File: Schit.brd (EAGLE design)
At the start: 58.1 x 47 mm, 15 parts, among them IC2 MEGA16-A, Q1 12M

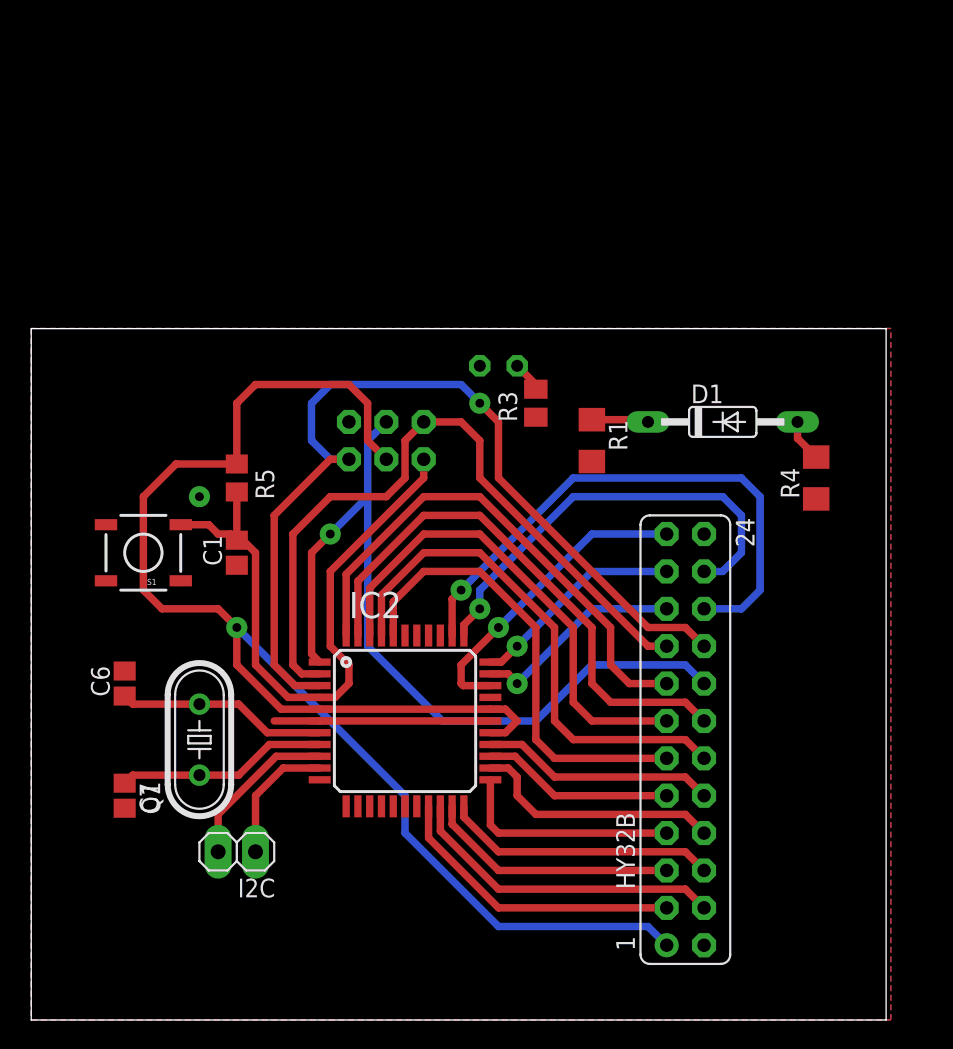
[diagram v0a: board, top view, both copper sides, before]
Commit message: change mc to ATMega64A
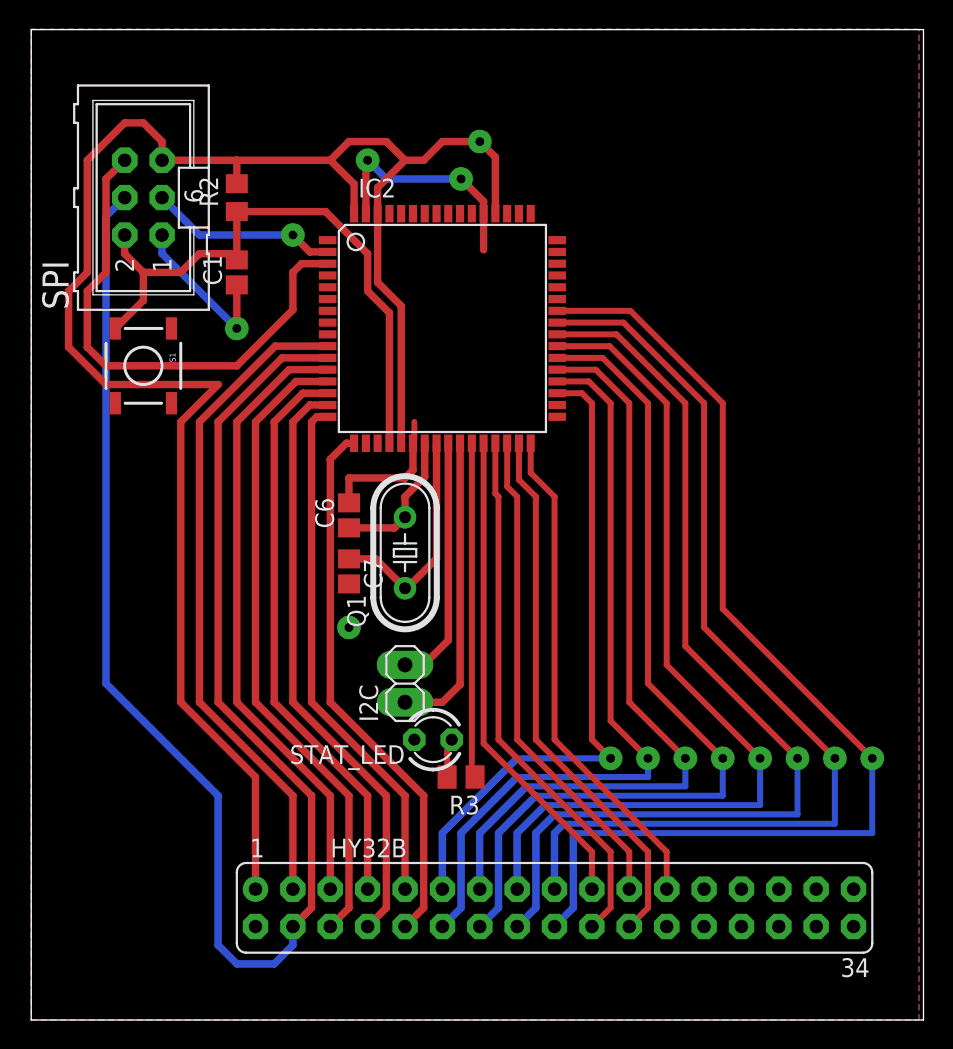
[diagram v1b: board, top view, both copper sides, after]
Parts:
- removed D1: 1N4446, diode:DO35-10
- removed R1: 220, resistor:R1206
- removed R4: 20, resistor:R1206
- removed R5: 10k, rcl:R0805
- added R2: 10k, rcl:R0805
- HY32B: device con-lsta:FE12-2 -> con-lsta:FE17-2
- IC2: value MEGA16-A -> MEGA64-A; device atmel:TQFP44 -> atmel:TQFP64
- moved IC2 26.8 mm to (27.9, 47.0)
- moved R3 25.9 mm to (29.2, 16.5), turned to 180 degrees
- moved STAT_LED 25.8 mm to (27.3, 19.1), flipped to the top, turned to 180 degrees
- moved SPI 23.3 mm to (7.62, 55.9), flipped to the top, turned to 90 degrees
- moved C7 21.6 mm to (21.6, 30.5)
- moved C6 19.1 mm to (21.6, 34.3)
- moved C1 19.0 mm to (14.0, 50.8)
- moved Q1 18.9 mm to (25.4, 31.8)
- moved I2C 16.2 mm to (25.4, 22.9), turned to 90 degrees
- moved HY32B 14.5 mm to (35.6, 7.62), turned to 0 degrees
- moved S1 12.7 mm to (7.62, 44.5), turned to 270 degrees
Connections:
- net GND1 renamed N$72
- removed net GND2: IC2.39
- removed net N$10: IC2.12
- removed net N$11: IC2.13
- removed net N$12: IC2.14
- removed net N$13: IC2.15
- removed net N$14: IC2.16
- removed net N$2: D1.A, R4.2
- removed net N$3: I2C.2, IC2.9
- removed net N$4: I2C.1, IC2.10
- removed net N$42: IC2.30
- removed net N$8: IC2.11
- removed net VCC1: IC2.17
- removed net VCC2: IC2.38
- removed net XTAL1: C6.1, IC2.7, Q1.2
- new net MISO: IC2.3, SPI.6
- new net MOSI: IC2.2, SPI.3
- new net N$23: IC2.4
- new net N$24: IC2.5
- new net N$25: IC2.6
- new net N$26: IC2.7
- new net N$27: IC2.8
- new net N$28: IC2.9
- new net N$30: C6.1, IC2.23, Q1.2
- new net N$54: IC2.51
- new net N$55: IC2.50
- new net N$56: IC2.49
- new net N$57: IC2.48
- new net N$58: IC2.47
- new net N$59: IC2.46
- new net N$60: IC2.45
- new net N$61: IC2.44
- new net N$73: IC2.19
- new net N$74: IC2.43
- new net N$75: IC2.34
- new net N$76: IC2.33
- new net N$77: IC2.1
- new net N$78: IC2.54
- new net N$79: IC2.55
- new net N$80: IC2.56
- new net N$81: IC2.57
- new net N$82: IC2.58
- new net N$83: IC2.59
- new net N$84: IC2.60
- new net N$85: IC2.61
- new net SCL: I2C.2, IC2.25
- new net SDA: I2C.1, IC2.26
- net CS: now also IC2.28; no longer IC2.32
- net D0: now also IC2.10; no longer IC2.19
- net D1: now also IC2.11, SPI.4; no longer IC2.20
- net D10: now also IC2.37; no longer IC2.42
- net D11: now also IC2.38; no longer IC2.43
- net D12: now also IC2.39; no longer IC2.44
- net D13: now also IC2.40; no longer IC2.1, SPI.4
- net D14: now also IC2.41; no longer IC2.2, SPI.2
- net D15: now also IC2.42; no longer IC2.3, SPI.5
- net D2: now also IC2.12; no longer IC2.21
- net D3: now also IC2.13; no longer IC2.22
- net D4: now also IC2.14; no longer IC2.23
- net D5: now also IC2.15; no longer IC2.24
- net D6: now also IC2.16; no longer IC2.25
- net D7: now also IC2.17; no longer IC2.26
- net D8: now also IC2.35; no longer IC2.40
- net D9: now also IC2.36; no longer IC2.41
- net GND: now also IC2.22, IC2.53, IC2.63, SPI.1; no longer IC2.28, IC2.6, R4.1, SPI.6
- net N$1: now also IC2.27, R3.1; no longer D1.C, R1.1
- net N$29: now also IC2.24; no longer IC2.8
- net RD: now also IC2.31; no longer IC2.34
- net RS: now also IC2.29; no longer IC2.35
- net RST: now also IC2.32; no longer IC2.31
- net SPI_RST: now also IC2.20, R2.1, SPI.2; no longer IC2.4, R5.2, SPI.1
- net VCC: now also IC2.21, IC2.52, IC2.62, IC2.64, R2.2, SPI.5; no longer IC2.27, IC2.29, IC2.5, R5.1, SPI.3
- net WR: now also IC2.30; no longer IC2.33
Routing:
- net D1: track 21.8 -> 108.6 mm
- net MISO: track 0.00 -> 35.0 mm
- net D12: track 34.9 -> 60.1 mm, vias 0 -> 1
- net D0: track 20.3 -> 45.2 mm
- net D3: track 18.6 -> 43.5 mm
- net D2: track 17.1 -> 42.0 mm
- net D4: track 15.3 -> 38.8 mm
- net D5: track 17.1 -> 40.3 mm
- net D6: track 13.1 -> 35.6 mm
- net D11: track 37.1 -> 59.4 mm, vias 0 -> 1
- net GND: track 14.7 -> 36.8 mm, vias 1 -> 4
- net D7: track 16.0 -> 37.0 mm
- net SDA: track 0.00 -> 20.6 mm
- net VCC: track 104.4 -> 124.9 mm
- net D10: track 33.2 -> 52.6 mm, vias 0 -> 1
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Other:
- board size 58.1 x 47 mm -> 60.6 x 67.3 mm

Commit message: change mc to ATmega128A
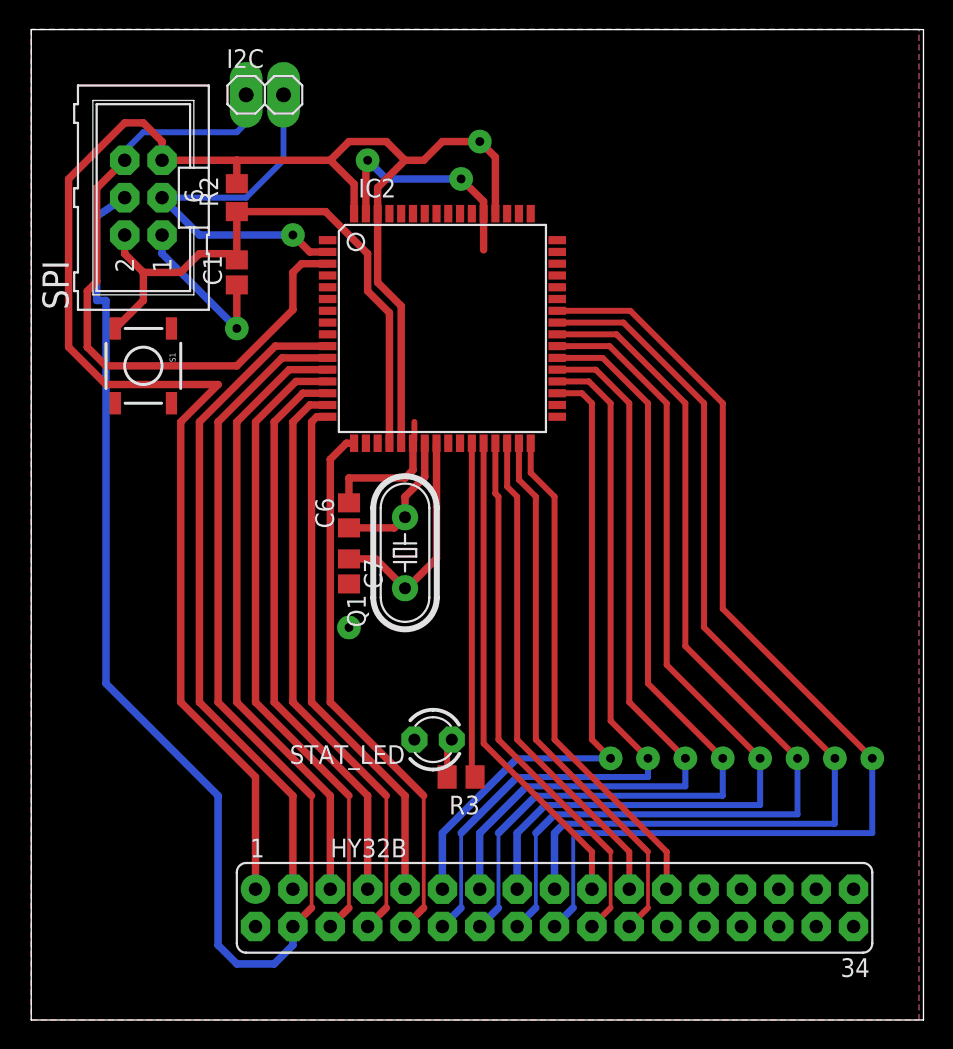
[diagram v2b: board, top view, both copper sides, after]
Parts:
- IC2: value MEGA64-A -> MEGA128-A
- moved I2C 41.1 mm to (15.9, 62.9), turned to 0 degrees
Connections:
- net MISO: now also I2C.1
- net MOSI: now also I2C.2
- net SCL: no longer I2C.2
- net SDA: no longer I2C.1
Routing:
- net SDA: track 20.6 -> 0.00 mm
- net SCL: track 17.0 -> 0.00 mm
- net MOSI: track 12.8 -> 26.5 mm
- net MISO: track 35.0 -> 46.6 mm
- net D1: track 108.6 -> 109.7 mm
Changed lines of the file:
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@@
 <param name="msMicroVia" value="9.99mm"/>
 <param name="msBlindViaRatio" value="0.5"/>
-<param name="rvPadTop" value="0.45"/>
+<param name="rvPadTop" value="0.6"/>
 <param name="rvPadInner" value="0.3"/>
-<param name="rvPadBottom" value="0.45"/>
+<param name="rvPadBottom" value="0.6"/>
 <param name="rvViaOuter" value="1"/>
 <param name="rvViaInner" value="1"/>
@@
 <param name="rvMicroViaInner" value="0.25"/>
 <param name="rlMinPadTop" value="10mil"/>
-<param name="rlMaxPadTop" value="20mil"/>
+<param name="rlMaxPadTop" value="30mil"/>
 <param name="rlMinPadInner" value="10mil"/>
 <param name="rlMaxPadInner" value="20mil"/>
 <param name="rlMinPadBottom" value="10mil"/>
-<param name="rlMaxPadBottom" value="20mil"/>
+<param name="rlMaxPadBottom" value="30mil"/>
 <param name="rlMinViaOuter" value="8mil"/>
 <param name="rlMaxViaOuter" value="20mil"/>
@@
 <element name="STAT_LED" library="led" package="LED3MM" value="" x="27.305" y="19.05" rot="R180"/>
 <element name="R3" library="rcl" package="M2012" value="220" x="29.21" y="16.51" rot="R180"/>
-<element name="I2C" library="pinhead" package="1X02" value="" x="25.4" y="22.86" rot="R90"/>
-<element name="IC2" library="atmel" package="TQFP64" value="MEGA64-A" x="27.94" y="46.99">
-<attribute name="OC_NEWARK" value="01M6899" x="27.94" y="46.99" size="1.778" layer="27" display="off"/>
-<attribute name="MPN" value="ATMEGA64-16AU" x="27.94" y="46.99" size="1.778" layer="27" display="off"/>
+<element name="I2C" library="pinhead" package="1X02" value="" x="15.875" y="62.865"/>
+<element name="IC2" library="atmel" package="TQFP64" value="MEGA128-A" x="27.94" y="46.99">
+<attribute name="OC_NEWARK" value="95K7364" x="27.94" y="46.99" size="1.778" layer="27" display="off"/>
+<attribute name="MPN" value="ATMEGA128-16AU" x="27.94" y="46.99" size="1.778" layer="27" display="off"/>
 <attribute name="MF" value="" x="27.94" y="46.99" size="1.778" layer="27" display="off"/>
-<attribute name="OC_FARNELL" value="9171355" x="27.94" y="46.99" size="1.778" layer="27" display="off"/>
+<attribute name="OC_FARNELL" value="9171118" x="27.94" y="46.99" size="1.778" layer="27" display="off"/>
 </element>
 <element name="C1" library="rcl" package="C0805" value="0.1u" x="13.97" y="50.8" rot="R90"/>
@@
 <wire x1="12.7" y1="43.18" x2="5.08" y2="43.18" width="0.508" layer="1"/>
 <wire x1="5.08" y1="43.18" x2="2.54" y2="45.72" width="0.508" layer="1"/>
-<wire x1="2.54" y1="45.72" x2="2.54" y2="49.53" width="0.508" layer="1"/>
-<wire x1="2.54" y1="49.53" x2="3.81" y2="50.8" width="0.508" layer="1"/>
-<wire x1="3.81" y1="50.8" x2="3.81" y2="58.42" width="0.508" layer="1"/>
-<wire x1="3.81" y1="58.42" x2="6.35" y2="60.96" width="0.508" layer="1"/>
+<wire x1="2.54" y1="45.72" x2="2.54" y2="57.15" width="0.508" layer="1"/>
+<wire x1="2.54" y1="57.15" x2="6.35" y2="60.96" width="0.508" layer="1"/>
 <wire x1="6.35" y1="60.96" x2="7.62" y2="60.96" width="0.508" layer="1"/>
 <wire x1="7.62" y1="60.96" x2="8.89" y2="59.69" width="0.508" layer="1"/>
@@
 <wire x1="12.7" y1="21.59" x2="19.05" y2="15.24" width="0.508" layer="1"/>
 <wire x1="12.7" y1="40.64" x2="12.7" y2="21.59" width="0.508" layer="1"/>
-<wire x1="19.05" y1="15.24" x2="19.05" y2="7.62" width="0.508" layer="1"/>
+<wire x1="19.05" y1="15.24" x2="19.05" y2="7.62" width="0.254" layer="1"/>
 <wire x1="19.05" y1="7.62" x2="17.78" y2="6.35" width="0.508" layer="1"/>
 <contactref element="SPI" pad="4"/>
-<wire x1="6.35" y1="55.88" x2="5.08" y2="54.61" width="0.508" layer="16"/>
-<wire x1="5.08" y1="54.61" x2="5.08" y2="22.86" width="0.508" layer="16"/>
+<wire x1="6.35" y1="55.88" x2="4.445" y2="54.61" width="0.508" layer="16"/>
+<wire x1="4.445" y1="54.61" x2="4.445" y2="48.895" width="0.508" layer="16"/>
+<wire x1="4.445" y1="48.895" x2="5.08" y2="48.895" width="0.508" layer="16"/>
+<wire x1="5.08" y1="48.895" x2="5.08" y2="22.86" width="0.508" layer="16"/>
 <wire x1="5.08" y1="22.86" x2="12.7" y2="15.24" width="0.508" layer="16"/>
 <wire x1="12.7" y1="15.24" x2="12.7" y2="5.08" width="0.508" layer="16"/>
@@
 <wire x1="15.24" y1="40.64" x2="15.24" y2="21.59" width="0.508" layer="1"/>
 <wire x1="15.24" y1="21.59" x2="21.59" y2="15.24" width="0.508" layer="1"/>
-<wire x1="21.59" y1="15.24" x2="21.59" y2="7.62" width="0.508" layer="1"/>
+<wire x1="21.59" y1="15.24" x2="21.59" y2="7.62" width="0.254" layer="1"/>
 <wire x1="21.59" y1="7.62" x2="20.32" y2="6.35" width="0.508" layer="1"/>
 </signal>
@@
 <wire x1="17.78" y1="40.64" x2="17.78" y2="21.59" width="0.508" layer="1"/>
 <wire x1="17.78" y1="21.59" x2="24.13" y2="15.24" width="0.508" layer="1"/>
-<wire x1="24.13" y1="15.24" x2="24.13" y2="7.62" width="0.508" layer="1"/>
+<wire x1="24.13" y1="15.24" x2="24.13" y2="7.62" width="0.254" layer="1"/>
 <wire x1="24.13" y1="7.62" x2="22.86" y2="6.35" width="0.508" layer="1"/>
 </signal>
@@
 <wire x1="20.32" y1="38.1" x2="20.32" y2="21.59" width="0.508" layer="1"/>
 <wire x1="20.32" y1="21.59" x2="26.67" y2="15.24" width="0.508" layer="1"/>
-<wire x1="26.67" y1="15.24" x2="26.67" y2="7.62" width="0.508" layer="1"/>
+<wire x1="26.67" y1="15.24" x2="26.67" y2="7.62" width="0.254" layer="1"/>
 <wire x1="26.67" y1="7.62" x2="25.4" y2="6.35" width="0.508" layer="1"/>
 </signal>
@@
 <wire x1="41.91" y1="16.51" x2="33.02" y2="16.51" width="0.4064" layer="16"/>
 <wire x1="33.02" y1="16.51" x2="29.21" y2="12.7" width="0.508" layer="16"/>
-<wire x1="29.21" y1="12.7" x2="29.21" y2="7.62" width="0.508" layer="16"/>
+<wire x1="29.21" y1="12.7" x2="29.21" y2="7.62" width="0.254" layer="16"/>
 <wire x1="29.21" y1="7.62" x2="27.94" y2="6.35" width="0.508" layer="16"/>
 </signal>
@@
 <wire x1="46.99" y1="15.24" x2="34.29" y2="15.24" width="0.4064" layer="16"/>
 <wire x1="34.29" y1="15.24" x2="31.75" y2="12.7" width="0.508" layer="16"/>
-<wire x1="31.75" y1="12.7" x2="31.75" y2="7.62" width="0.508" layer="16"/>
+<wire x1="31.75" y1="12.7" x2="31.75" y2="7.62" width="0.254" layer="16"/>
 <wire x1="31.75" y1="7.62" x2="30.48" y2="6.35" width="0.508" layer="16"/>
 </signal>
@@
 <wire x1="52.07" y1="13.97" x2="35.56" y2="13.97" width="0.4064" layer="16"/>
 <wire x1="35.56" y1="13.97" x2="34.29" y2="12.7" width="0.508" layer="16"/>
-<wire x1="34.29" y1="12.7" x2="34.29" y2="7.62" width="0.508" layer="16"/>
+<wire x1="34.29" y1="12.7" x2="34.29" y2="7.62" width="0.254" layer="16"/>
 <wire x1="34.29" y1="7.62" x2="33.02" y2="6.35" width="0.508" layer="16"/>
 </signal>
@@
 <wire x1="57.15" y1="17.78" x2="57.15" y2="12.7" width="0.4064" layer="16"/>
 <wire x1="57.15" y1="12.7" x2="36.83" y2="12.7" width="0.4064" layer="16"/>
-<wire x1="36.83" y1="12.7" x2="36.83" y2="7.62" width="0.508" layer="16"/>
+<wire x1="36.83" y1="12.7" x2="36.83" y2="7.62" width="0.254" layer="16"/>
 <wire x1="36.83" y1="7.62" x2="35.56" y2="6.35" width="0.508" layer="16"/>
 </signal>
@@
 <wire x1="31.75" y1="35.56" x2="31.75" y2="19.05" width="0.4064" layer="1"/>
 <wire x1="31.75" y1="19.05" x2="39.37" y2="11.43" width="0.4064" layer="1"/>
-<wire x1="39.37" y1="11.43" x2="39.37" y2="7.62" width="0.4064" layer="1"/>
+<wire x1="39.37" y1="11.43" x2="39.37" y2="7.62" width="0.254" layer="1"/>
 <wire x1="39.37" y1="7.62" x2="38.1" y2="6.35" width="0.4064" layer="1"/>
 </signal>
@@
 <wire x1="34.29" y1="35.56" x2="34.29" y2="19.05" width="0.4064" layer="1"/>
 <wire x1="34.29" y1="19.05" x2="41.91" y2="11.43" width="0.4064" layer="1"/>
-<wire x1="41.91" y1="11.43" x2="41.91" y2="7.62" width="0.4064" layer="1"/>
+<wire x1="41.91" y1="11.43" x2="41.91" y2="7.62" width="0.254" layer="1"/>
 <wire x1="41.91" y1="7.62" x2="40.64" y2="6.35" width="0.4064" layer="1"/>
 </signal>
@@
 </signal>
 <signal name="SCL">
-<contactref element="I2C" pad="2"/>
 <contactref element="IC2" pad="25"/>
-<wire x1="25.4" y1="24.13" x2="26.67" y2="24.13" width="0.508" layer="1"/>
-<wire x1="26.67" y1="24.13" x2="28.34" y2="25.8" width="0.508" layer="1"/>
-<wire x1="28.34" y1="39.19" x2="28.34" y2="25.8" width="0.508" layer="1"/>
 </signal>
 <signal name="SDA">
-<contactref element="I2C" pad="1"/>
 <contactref element="IC2" pad="26"/>
-<wire x1="29.14" y1="39.19" x2="29.14" y2="22.79" width="0.508" layer="1"/>
-<wire x1="29.14" y1="22.79" x2="27.94" y2="21.59" width="0.508" layer="1"/>
-<wire x1="27.94" y1="21.59" x2="25.4" y2="21.59" width="0.508" layer="1"/>
 </signal>
 <signal name="MOSI">
@@
 <wire x1="17.78" y1="53.34" x2="11.43" y2="53.34" width="0.508" layer="16"/>
 <wire x1="11.43" y1="53.34" x2="8.89" y2="55.88" width="0.508" layer="16"/>
+<contactref element="I2C" pad="2"/>
+<wire x1="17.145" y1="62.865" x2="17.145" y2="58.42" width="0.4064" layer="16"/>
+<wire x1="17.145" y1="58.42" x2="14.605" y2="55.88" width="0.4064" layer="16"/>
+<wire x1="14.605" y1="55.88" x2="8.89" y2="55.88" width="0.4064" layer="16"/>
 </signal>
 <signal name="MISO">
@@
 <wire x1="5.08" y1="44.45" x2="3.81" y2="45.72" width="0.508" layer="1"/>
 <wire x1="3.81" y1="45.72" x2="3.81" y2="49.53" width="0.508" layer="1"/>
-<wire x1="3.81" y1="49.53" x2="5.08" y2="50.8" width="0.508" layer="1"/>
-<wire x1="5.08" y1="50.8" x2="5.08" y2="57.15" width="0.508" layer="1"/>
-<wire x1="5.08" y1="57.15" x2="6.35" y2="58.42" width="0.508" layer="1"/>
+<wire x1="3.81" y1="49.53" x2="4.445" y2="50.165" width="0.508" layer="1"/>
+<wire x1="4.445" y1="50.165" x2="4.445" y2="56.515" width="0.508" layer="1"/>
+<wire x1="4.445" y1="56.515" x2="6.35" y2="58.42" width="0.508" layer="1"/>
+<contactref element="I2C" pad="1"/>
+<wire x1="6.35" y1="58.42" x2="6.35" y2="59.055" width="0.4064" layer="16"/>
+<wire x1="6.35" y1="59.055" x2="7.62" y2="60.325" width="0.4064" layer="16"/>
+<wire x1="7.62" y1="60.325" x2="13.97" y2="60.325" width="0.4064" layer="16"/>
+<wire x1="13.97" y1="60.325" x2="14.605" y2="60.96" width="0.4064" layer="16"/>
+<wire x1="14.605" y1="60.96" x2="14.605" y2="62.865" width="0.4064" layer="16"/>
 </signal>
 <signal name="N$23">
